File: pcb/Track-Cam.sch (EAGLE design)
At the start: 44 parts, among them IC1 STM32F042KT/M, IC2 BD6211F/M, IC3 BD6211F/M, P1 RASPI_BOARD_B+#_HC

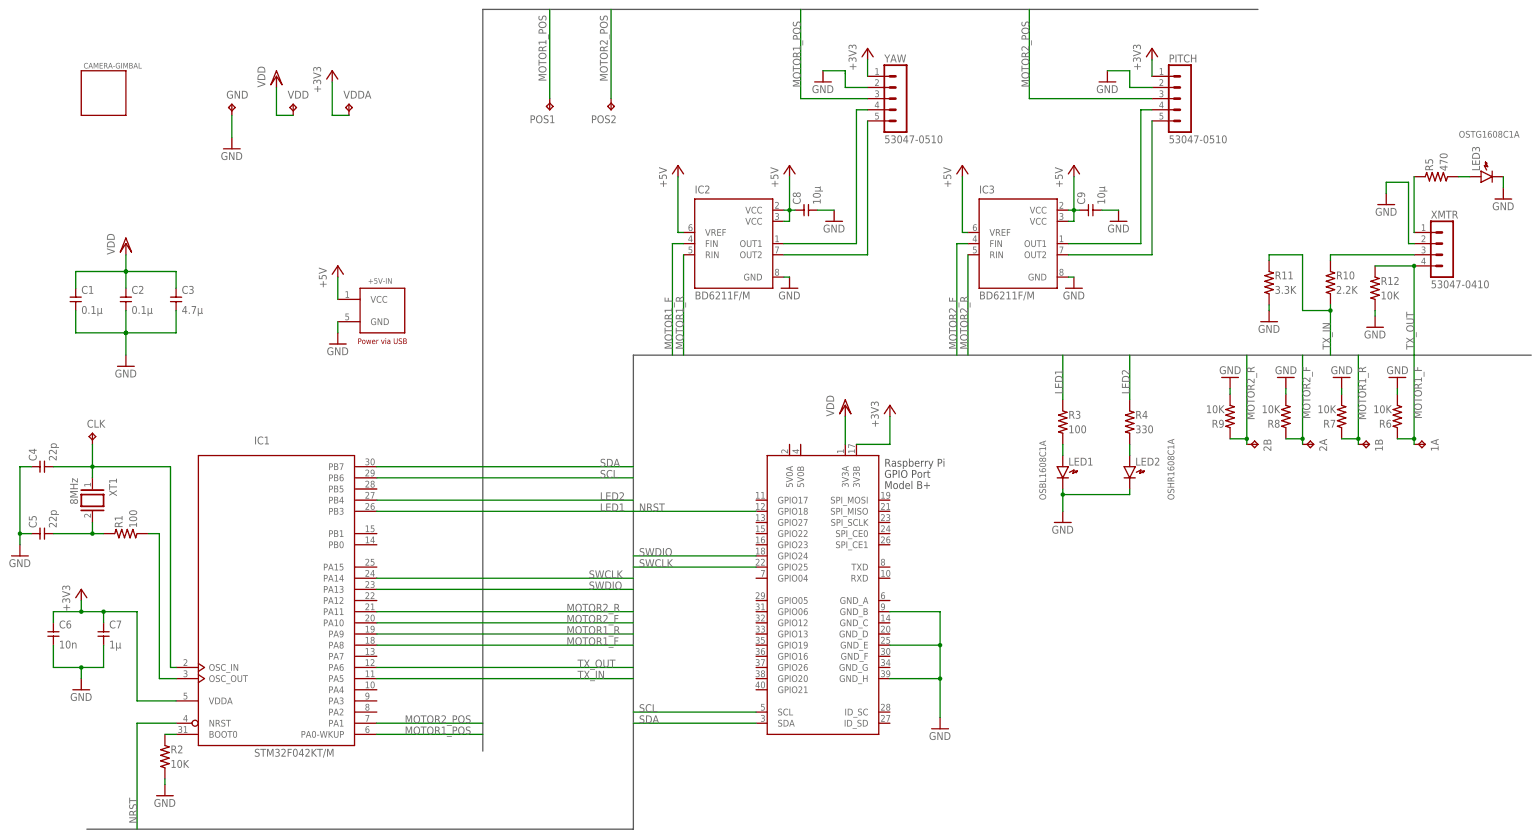
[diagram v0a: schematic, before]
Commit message: change pcb design as connecting with Rasbery Pi by SPI
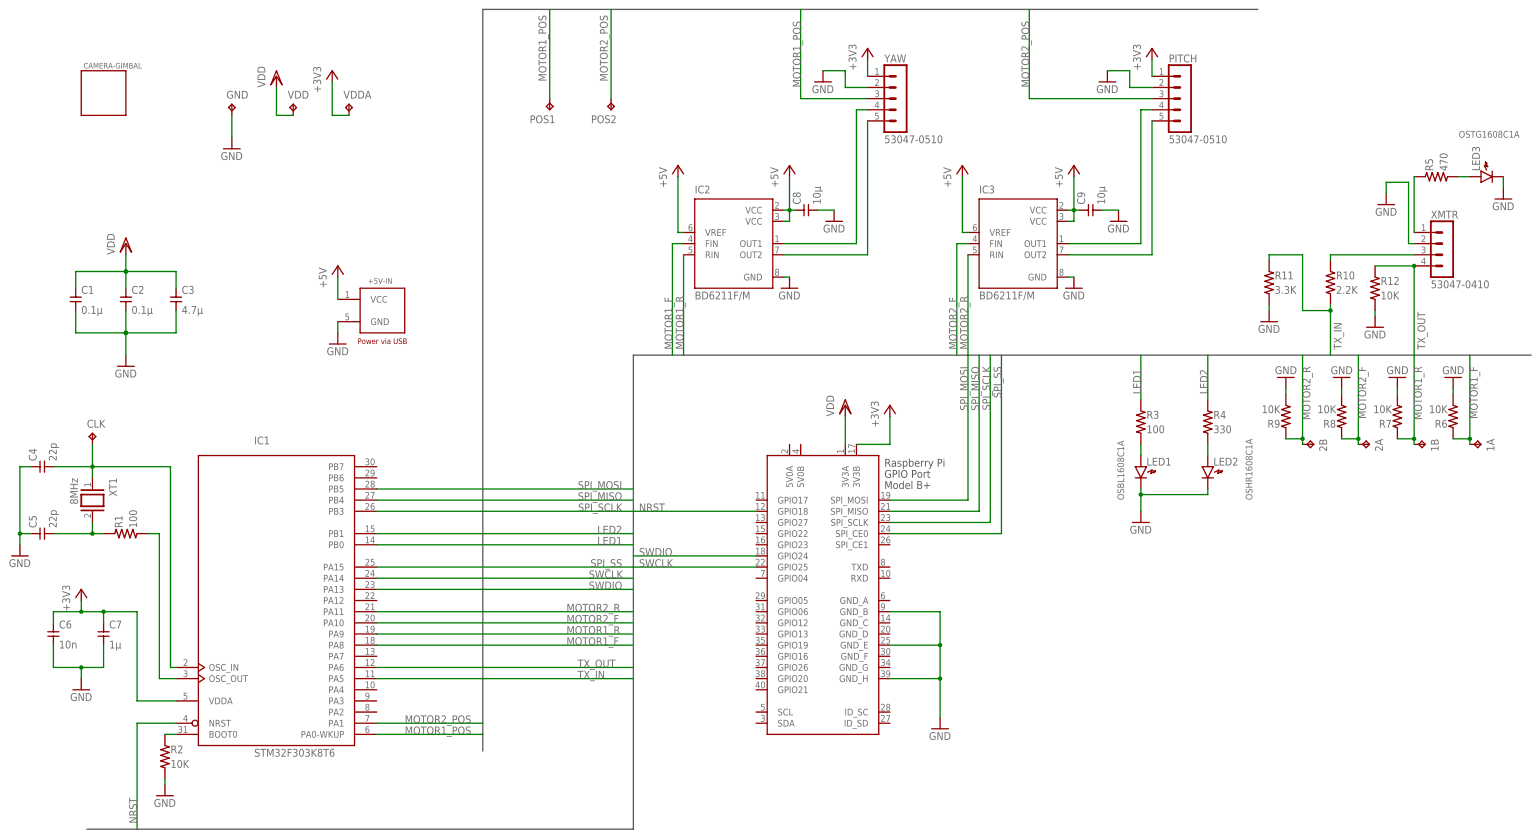
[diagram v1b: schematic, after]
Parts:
- IC1: value STM32F042KT/M -> STM32F303K8T6
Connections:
- removed net SCL: IC1MCU.PB6, P1.SCL
- removed net SDA: IC1MCU.PB7, P1.SDA
- new net SPI_MISO: IC1MCU.PB4, P1.SPI_MISO
- new net SPI_MOSI: IC1MCU.PB5, P1.SPI_MOSI
- new net SPI_SCLK: IC1MCU.PB3, P1.SPI_SCLK
- new net SPI_SS: IC1MCU.PA15, P1.SPI_CE0
- net LED1: now also IC1MCU.PB0; no longer IC1MCU.PB3
- net LED2: now also IC1MCU.PB1; no longer IC1MCU.PB4
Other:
- moved on the sheet: 1A, 1B, 2A, 2B, LED1, LED2, R3, R4, R6, R7, R8, R9

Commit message: optimize pcb design to suport 3D model
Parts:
- C1, C2, C3, C6, C7, C8, C9: device gen-discrete:CAPACITOR2012 -> gen-discrete2:CAPACITOR2012
- C4, C5: device gen-discrete:CAPACITOR1608 -> gen-discrete2:CAPACITOR1608
